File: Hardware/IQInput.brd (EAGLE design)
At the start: 50 x 50 mm, 97 parts, among them IC1 TPS60403, IC2 LT1819, IC3 AD8132, IC4 AD8132, IC5 MAX19515, IC6 PCA9555BS, K1 FTR-B4G, K2 FTR-B4G, K3 FTR-B4G, K4 FTR-B4G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

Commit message: Added value to input protection resistor
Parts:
- R14, R28: value (none) -> 10k
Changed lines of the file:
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@@
 <layer number="14" name="Route14" color="22" fill="1" visible="no" active="no"/>
 <layer number="15" name="Route15" color="14" fill="1" visible="no" active="yes"/>
-<layer number="16" name="Bottom" color="1" fill="1" visible="no" active="yes"/>
+<layer number="16" name="Bottom" color="1" fill="1" visible="yes" active="yes"/>
 <layer number="17" name="Pads" color="2" fill="1" visible="yes" active="yes"/>
 <layer number="18" name="Vias" color="2" fill="1" visible="yes" active="yes"/>
@@
 <layer number="20" name="Dimension" color="24" fill="1" visible="yes" active="yes"/>
 <layer number="21" name="tPlace" color="7" fill="1" visible="yes" active="yes"/>
-<layer number="22" name="bPlace" color="7" fill="1" visible="no" active="yes"/>
+<layer number="22" name="bPlace" color="7" fill="1" visible="yes" active="yes"/>
 <layer number="23" name="tOrigins" color="15" fill="1" visible="yes" active="yes"/>
-<layer number="24" name="bOrigins" color="15" fill="1" visible="no" active="yes"/>
+<layer number="24" name="bOrigins" color="15" fill="1" visible="yes" active="yes"/>
 <layer number="25" name="tNames" color="7" fill="1" visible="no" active="yes"/>
 <layer number="26" name="bNames" color="7" fill="1" visible="no" active="yes"/>
@@
 <layer number="28" name="bValues" color="7" fill="1" visible="no" active="yes"/>
 <layer number="29" name="tStop" color="7" fill="3" visible="yes" active="yes"/>
-<layer number="30" name="bStop" color="7" fill="6" visible="no" active="yes"/>
+<layer number="30" name="bStop" color="7" fill="6" visible="yes" active="yes"/>
 <layer number="31" name="tCream" color="7" fill="4" visible="no" active="yes"/>
 <layer number="32" name="bCream" color="7" fill="5" visible="no" active="yes"/>
@@
 <layer number="38" name="bTest" color="7" fill="1" visible="no" active="yes"/>
 <layer number="39" name="tKeepout" color="4" fill="11" visible="yes" active="yes"/>
-<layer number="40" name="bKeepout" color="1" fill="11" visible="no" active="yes"/>
+<layer number="40" name="bKeepout" color="1" fill="11" visible="yes" active="yes"/>
 <layer number="41" name="tRestrict" color="4" fill="10" visible="yes" active="yes"/>
-<layer number="42" name="bRestrict" color="1" fill="10" visible="no" active="yes"/>
+<layer number="42" name="bRestrict" color="1" fill="10" visible="yes" active="yes"/>
 <layer number="43" name="vRestrict" color="2" fill="10" visible="no" active="yes"/>
 <layer number="44" name="Drills" color="7" fill="1" visible="no" active="yes"/>
 <layer number="45" name="Holes" color="7" fill="1" visible="no" active="yes"/>
-<layer number="46" name="Milling" color="3" fill="1" visible="no" active="yes"/>
+<layer number="46" name="Milling" color="3" fill="1" visible="yes" active="yes"/>
 <layer number="47" name="Measures" color="7" fill="1" visible="no" active="yes"/>
 <layer number="48" name="Document" color="7" fill="1" visible="no" active="yes"/>
@@
 <layer number="50" name="dxf" color="7" fill="1" visible="no" active="no"/>
 <layer number="51" name="tDocu" color="7" fill="1" visible="yes" active="yes"/>
-<layer number="52" name="bDocu" color="7" fill="1" visible="no" active="yes"/>
+<layer number="52" name="bDocu" color="7" fill="1" visible="yes" active="yes"/>
 <layer number="53" name="tPadExt" color="7" fill="1" visible="no" active="no"/>
 <layer number="54" name="bPadExt" color="1" fill="1" visible="no" active="no"/>
@@
 <attribute name="VALUE" x="18.695" y="48.135" size="1.27" layer="27" rot="R270"/>
 </element>
-<element name="R14" library="rcl" package="R0603" value="" x="32.2" y="32.4" smashed="yes">
+<element name="R14" library="rcl" package="R0603" value="10k" x="32.2" y="32.4" smashed="yes">
 <attribute name="NAME" x="33.865" y="32.335" size="1.016" layer="25" font="vector"/>
 <attribute name="VALUE" x="31.565" y="30.495" size="1.27" layer="27"/>
@@
 <attribute name="VALUE" x="38.095" y="41.635" size="1.27" layer="27" rot="R270"/>
 </element>
-<element name="R28" library="rcl" package="R0603" value="" x="32.2" y="34.4" smashed="yes">
+<element name="R28" library="rcl" package="R0603" value="10k" x="32.2" y="34.4" smashed="yes">
 <attribute name="NAME" x="33.865" y="33.535" size="1.016" layer="25" font="vector"/>
 <attribute name="VALUE" x="31.565" y="32.495" size="1.27" layer="27"/>

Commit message: Specified values
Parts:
- C1, C7: value (none) -> 100n
- C10, C3, C4, C9: value (none) -> DNP
- C2, C8: value (none) -> 100p
- L1, L2: value (none) -> Ferrite
- R1, R15, R16, R2: value (none) -> 49R9
- R17, R18, R19, R20, R3, R4, R5, R6: value (none) -> 470
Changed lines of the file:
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@@
 </autorouter>
 <elements>
-<element name="C1" library="rcl" package="C0603" value="" x="25.5" y="15.5" smashed="yes" rot="R180">
+<element name="C1" library="rcl" package="C0603" value="100n" x="25.5" y="15.5" smashed="yes" rot="R180">
 <attribute name="NAME" x="26.135" y="14.665" size="1.016" layer="25" font="vector" rot="R180"/>
 <attribute name="VALUE" x="26.135" y="17.405" size="1.27" layer="27" rot="R180"/>
 </element>
-<element name="C10" library="rcl" package="C0603" value="" x="36" y="21" smashed="yes" rot="R270">
+<element name="C10" library="rcl" package="C0603" value="DNP" x="36" y="21" smashed="yes" rot="R270">
 <attribute name="NAME" x="46" y="11.2" size="1.016" layer="25" font="vector" rot="R270"/>
 <attribute name="VALUE" x="34.095" y="21.635" size="1.27" layer="27" rot="R270"/>
@@
 <attribute name="VALUE" x="46.965" y="38.795" size="1.27" layer="27"/>
 </element>
-<element name="C2" library="rcl" package="C0603" value="" x="29" y="17.1" smashed="yes" rot="R180">
+<element name="C2" library="rcl" package="C0603" value="100p" x="29" y="17.1" smashed="yes" rot="R180">
 <attribute name="NAME" x="29.635" y="16.265" size="1.016" layer="25" font="vector" rot="R180"/>
 <attribute name="VALUE" x="29.635" y="19.005" size="1.27" layer="27" rot="R180"/>
@@
 <attribute name="VALUE" x="27.905" y="7.365" size="1.27" layer="27" rot="R90"/>
 </element>
-<element name="C3" library="rcl" package="C0603" value="" x="34" y="21" smashed="yes" rot="R270">
+<element name="C3" library="rcl" package="C0603" value="DNP" x="34" y="21" smashed="yes" rot="R270">
 <attribute name="NAME" x="43.3" y="11" size="1.016" layer="25" font="vector" rot="R270"/>
 <attribute name="VALUE" x="32.095" y="21.635" size="1.27" layer="27" rot="R270"/>
 </element>
-<element name="C4" library="rcl" package="C0603" value="" x="24" y="21" smashed="yes" rot="R270">
+<element name="C4" library="rcl" package="C0603" value="DNP" x="24" y="21" smashed="yes" rot="R270">
 <attribute name="NAME" x="22.135" y="21.435" size="1.016" layer="25" font="vector" rot="R270"/>
 <attribute name="VALUE" x="22.095" y="21.635" size="1.27" layer="27" rot="R270"/>
@@
 <attribute name="VALUE" x="34.365" y="22.995" size="1.27" layer="27"/>
 </element>
-<element name="C7" library="rcl" package="C0603" value="" x="35.5" y="17.1" smashed="yes" rot="R180">
+<element name="C7" library="rcl" package="C0603" value="100n" x="35.5" y="17.1" smashed="yes" rot="R180">
 <attribute name="NAME" x="36.835" y="16.365" size="1.016" layer="25" font="vector" rot="R180"/>
 <attribute name="VALUE" x="36.135" y="19.005" size="1.27" layer="27" rot="R180"/>
 </element>
-<element name="C8" library="rcl" package="C0603" value="" x="41.05" y="17.08" smashed="yes" rot="R180">
+<element name="C8" library="rcl" package="C0603" value="100p" x="41.05" y="17.08" smashed="yes" rot="R180">
 <attribute name="NAME" x="41.685" y="16.345" size="1.016" layer="25" font="vector" rot="R180"/>
 <attribute name="VALUE" x="41.685" y="18.985" size="1.27" layer="27" rot="R180"/>
 </element>
-<element name="C9" library="rcl" package="C0603" value="" x="46" y="21" smashed="yes" rot="R270">
+<element name="C9" library="rcl" package="C0603" value="DNP" x="46" y="21" smashed="yes" rot="R270">
 <attribute name="NAME" x="48.235" y="21.735" size="1.016" layer="25" font="vector" rot="R270"/>
 <attribute name="VALUE" x="44.095" y="21.635" size="1.27" layer="27" rot="R270"/>
@@
 <attribute name="VALUE" x="27.015" y="48.675" size="1.27" layer="27" rot="R270"/>
 </element>
-<element name="L1" library="rcl" package="L2012C" value="" x="48.5" y="37.5" smashed="yes" rot="R270">
+<element name="L1" library="rcl" package="L2012C" value="Ferrite" x="48.5" y="37.5" smashed="yes" rot="R270">
 <attribute name="NAME" x="46.77" y="37.605" size="1.016" layer="25" font="vector" rot="R270"/>
 <attribute name="VALUE" x="45.96" y="39.405" size="1.27" layer="27" rot="R270"/>
 </element>
-<element name="L2" library="rcl" package="L2012C" value="" x="44" y="37.5" smashed="yes" rot="R270">
+<element name="L2" library="rcl" package="L2012C" value="Ferrite" x="44" y="37.5" smashed="yes" rot="R270">
 <attribute name="NAME" x="44.97" y="37.305" size="1.016" layer="25" font="vector" rot="R270"/>
 <attribute name="VALUE" x="41.46" y="39.405" size="1.27" layer="27" rot="R270"/>
@@
 <attribute name="VALUE" x="7.54" y="18.31" size="1.27" layer="27" ratio="10" rot="R90"/>
 </element>
-<element name="R1" library="rcl" package="R0603" value="" x="30.9" y="18.7" smashed="yes" rot="R180">
+<element name="R1" library="rcl" package="R0603" value="49R9" x="30.9" y="18.7" smashed="yes" rot="R180">
 <attribute name="NAME" x="41.265" y="7.635" size="1.016" layer="25" font="vector"/>
 <attribute name="VALUE" x="31.535" y="20.605" size="1.27" layer="27" rot="R180"/>
@@
 <attribute name="VALUE" x="31.565" y="30.495" size="1.27" layer="27"/>
 </element>
-<element name="R15" library="rcl" package="R0603" value="" x="43" y="18.7" smashed="yes" rot="R180">
+<element name="R15" library="rcl" package="R0603" value="49R9" x="43" y="18.7" smashed="yes" rot="R180">
 <attribute name="NAME" x="47.335" y="19.165" size="1.016" layer="25" font="vector" rot="R180"/>
 <attribute name="VALUE" x="43.635" y="20.605" size="1.27" layer="27" rot="R180"/>
 </element>
-<element name="R16" library="rcl" package="R0603" value="" x="39.1" y="18.7" smashed="yes">
+<element name="R16" library="rcl" package="R0603" value="49R9" x="39.1" y="18.7" smashed="yes">
 <attribute name="NAME" x="47.165" y="7.635" size="1.016" layer="25" font="vector"/>
 <attribute name="VALUE" x="38.465" y="16.795" size="1.27" layer="27"/>
 </element>
-<element name="R17" library="rcl" package="R0603" value="" x="44.5" y="21" smashed="yes" rot="R270">
+<element name="R17" library="rcl" package="R0603" value="470" x="44.5" y="21" smashed="yes" rot="R270">
 <attribute name="NAME" x="46.935" y="22.135" size="1.016" layer="25" font="vector" rot="R270"/>
 <attribute name="VALUE" x="42.595" y="21.635" size="1.27" layer="27" rot="R270"/>
 </element>
-<element name="R18" library="rcl" package="R0603" value="" x="37.5" y="21" smashed="yes" rot="R270">
+<element name="R18" library="rcl" package="R0603" value="470" x="37.5" y="21" smashed="yes" rot="R270">
 <attribute name="NAME" x="47.3" y="11.3" size="1.016" layer="25" font="vector" rot="R270"/>
 <attribute name="VALUE" x="35.595" y="21.635" size="1.27" layer="27" rot="R270"/>
 </element>
-<element name="R19" library="rcl" package="R0603" value="" x="43.5" y="24" smashed="yes" rot="R270">
+<element name="R19" library="rcl" package="R0603" value="470" x="43.5" y="24" smashed="yes" rot="R270">
 <attribute name="NAME" x="48.635" y="25.235" size="1.016" layer="25" font="vector" rot="R270"/>
 <attribute name="VALUE" x="41.595" y="24.635" size="1.27" layer="27" rot="R270"/>
 </element>
-<element name="R2" library="rcl" package="R0603" value="" x="27.1" y="18.7" smashed="yes">
+<element name="R2" library="rcl" package="R0603" value="49R9" x="27.1" y="18.7" smashed="yes">
 <attribute name="NAME" x="25.565" y="16.935" size="1.016" layer="25" font="vector"/>
 <attribute name="VALUE" x="26.465" y="16.795" size="1.27" layer="27"/>
 </element>
-<element name="R20" library="rcl" package="R0603" value="" x="38.5" y="24" smashed="yes" rot="R270">
+<element name="R20" library="rcl" package="R0603" value="470" x="38.5" y="24" smashed="yes" rot="R270">
 <attribute name="NAME" x="45.465" y="22.865" size="1.016" layer="25" font="vector" rot="R90"/>
 <attribute name="VALUE" x="36.595" y="24.635" size="1.27" layer="27" rot="R270"/>
@@
 <attribute name="VALUE" x="3.095" y="36.035" size="1.27" layer="27" rot="R270"/>
 </element>
-<element name="R3" library="rcl" package="R0603" value="" x="32.5" y="21" smashed="yes" rot="R270">
+<element name="R3" library="rcl" package="R0603" value="470" x="32.5" y="21" smashed="yes" rot="R270">
 <attribute name="NAME" x="42" y="11" size="1.016" layer="25" font="vector" rot="R270"/>
 <attribute name="VALUE" x="30.595" y="21.635" size="1.27" layer="27" rot="R270"/>
@@
 <attribute name="VALUE" x="9.635" y="46.905" size="1.27" layer="27" rot="R180"/>
 </element>
-<element name="R4" library="rcl" package="R0603" value="" x="25.5" y="21" smashed="yes" rot="R270">
+<element name="R4" library="rcl" package="R0603" value="470" x="25.5" y="21" smashed="yes" rot="R270">
 <attribute name="NAME" x="24.435" y="19.435" size="1.016" layer="25" font="vector" rot="R270"/>
 <attribute name="VALUE" x="23.595" y="21.635" size="1.27" layer="27" rot="R270"/>
 </element>
-<element name="R5" library="rcl" package="R0603" value="" x="31.5" y="24" smashed="yes" rot="R270">
+<element name="R5" library="rcl" package="R0603" value="470" x="31.5" y="24" smashed="yes" rot="R270">
 <attribute name="NAME" x="24.635" y="24.735" size="1.016" layer="25" font="vector" rot="R270"/>
 <attribute name="VALUE" x="29.595" y="24.635" size="1.27" layer="27" rot="R270"/>
 </element>
-<element name="R6" library="rcl" package="R0603" value="" x="26.5" y="24" smashed="yes" rot="R270">
+<element name="R6" library="rcl" package="R0603" value="470" x="26.5" y="24" smashed="yes" rot="R270">
 <attribute name="NAME" x="21.035" y="24.135" size="1.016" layer="25" font="vector" rot="R270"/>
 <attribute name="VALUE" x="24.595" y="24.635" size="1.27" layer="27" rot="R270"/>

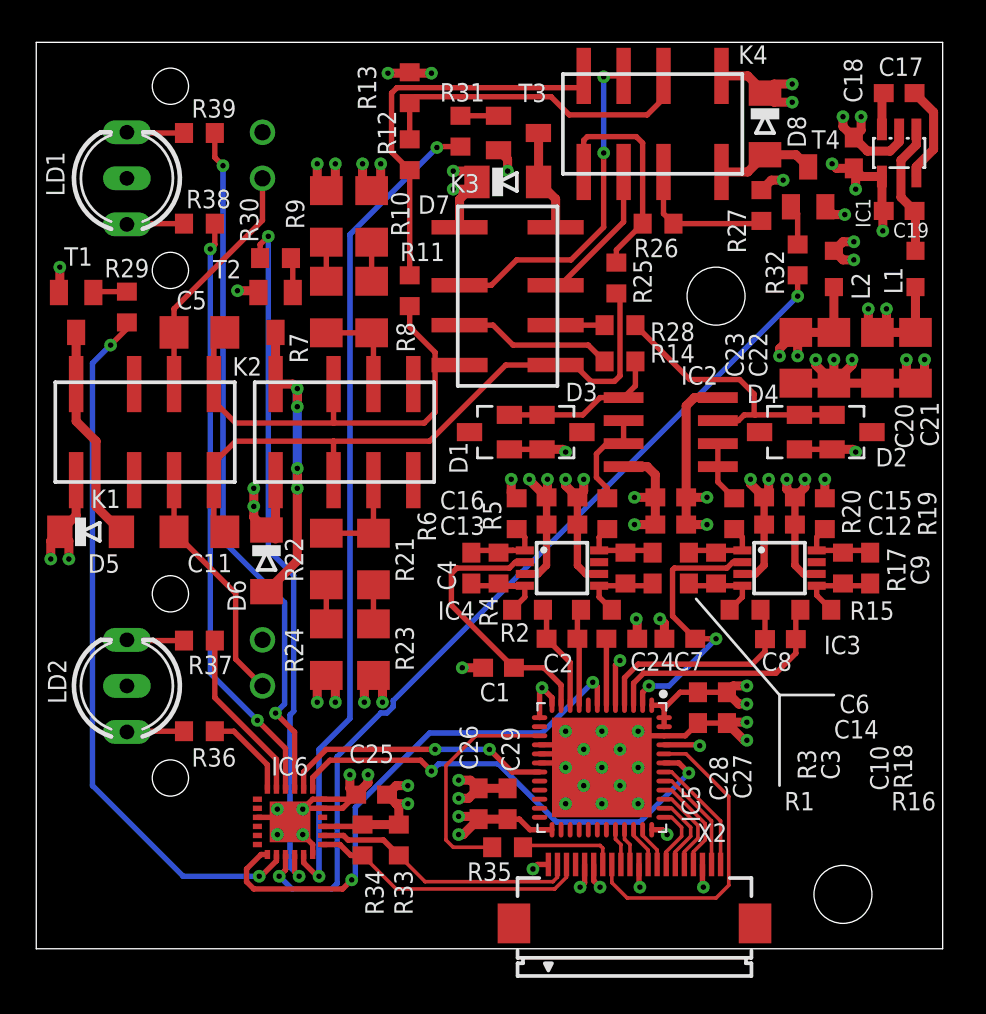
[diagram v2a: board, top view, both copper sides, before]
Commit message: Added testpoints, changes to silkscreen, created Gerber
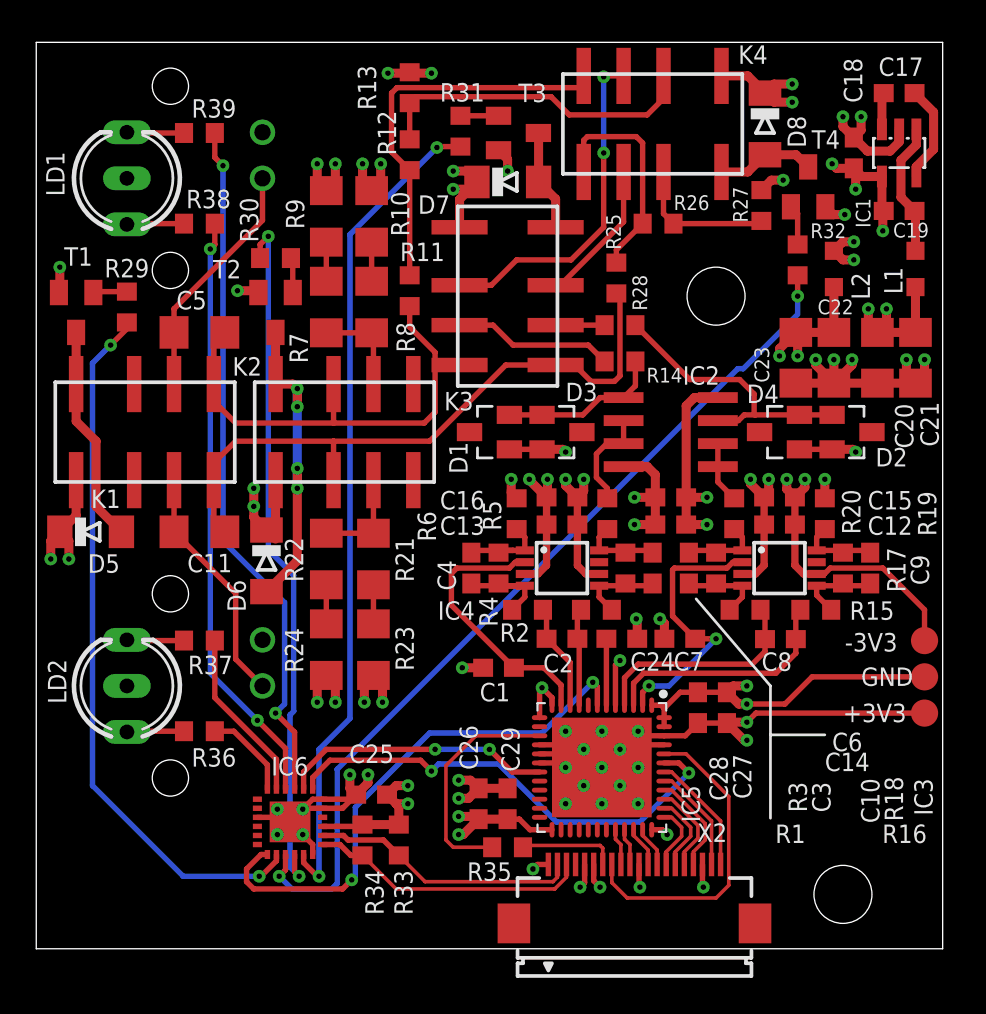
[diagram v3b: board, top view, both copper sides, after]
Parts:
- added TP1, TP2, TP3: TPTP15R, testpad:TP15R
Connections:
- net GND: now also IC5.45, TP2.TP
- net V+: now also TP1.TP; no longer IC5.45
- net V-: now also TP3.TP
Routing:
- net GND: track 100.3 -> 112.4 mm
- net V+: track 45.6 -> 54.5 mm, vias 13 -> 12
- net V-: track 33.4 -> 42.2 mm
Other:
- board text added: "+3V3"
- board text added: "-3V3"
- board text added: "10/2019"
- board text added: "GND"
